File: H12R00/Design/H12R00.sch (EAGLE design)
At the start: 32 parts, among them P1 HEXABIT_17.32_NO_P3_P6, U1 STM32F091CBU6, U2 AD628ARZ, X1 XTALL_CSTCE8M00G52

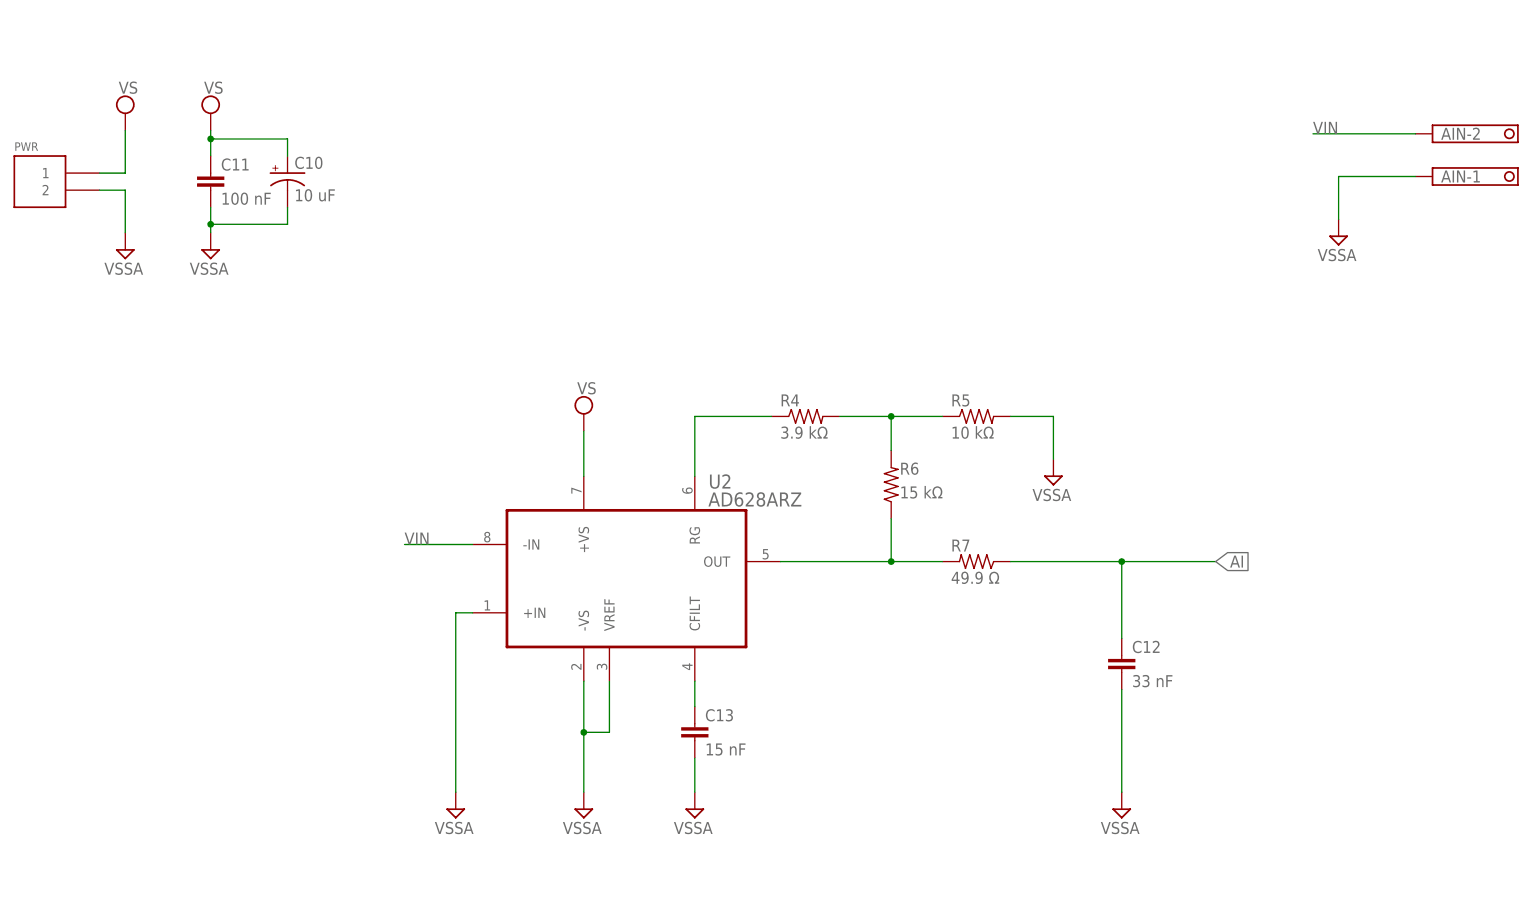
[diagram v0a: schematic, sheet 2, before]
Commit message: changed schematic design and modifies PCB (output files were not updated)
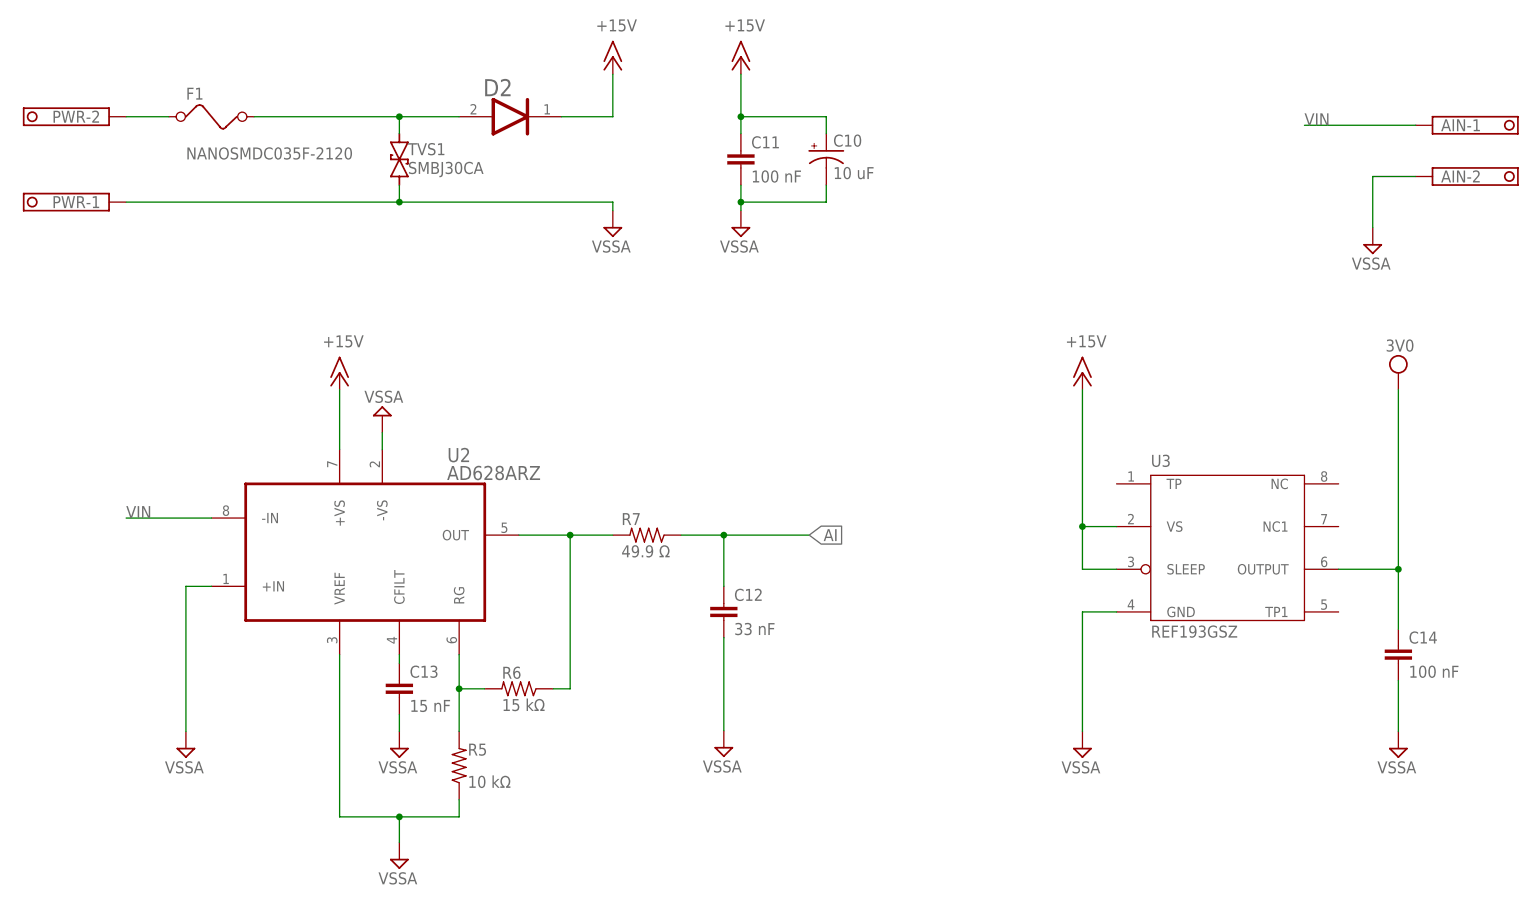
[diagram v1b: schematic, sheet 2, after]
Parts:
- removed FB1: FB-TDK_MMZ1608Y300B, Hexabitz:FB-TDK_MMZ1608Y300B
- removed R4: 3.9 kΩ, Hexabitz:R-0805
- added C14: 100 nF, Hexabitz:C-1206
- added D2: DIODES_SBR2U30P1-7DIODES_SBR2U30P1-7_0_0, Hexabitz:DIODES_SBR2U30P1-7DIODES_SBR2U30P1-7_0_0
- added F1: NANOSMDC035F-2120, Hexabitz:NANOSMDC035F-2120
- added TVS1: SMBJ30CA, Hexabitz:SMBJ30CA
- added U3: REF193GSZ, Hexabitz:REF193GSZ
- C13: CAPACITANCE 15 nF -> (none); MFN KEMET -> (none); MPN C0603C153J3GACTU -> (none); OCTOPART_URL https://octopart.com/c0603c153j3gactu-kemet-12793174 -> (none); TOLERANCE ±5% -> (none); VOLTAGE_RATING 25.0 V -> (none)
- PWR: value (none) -> CON-PHOENIX-350_1751248; device Hexabitz:1546111-2 -> Hexabitz:CON-PHOENIX-350_1751248
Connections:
- removed net AGND: AIN-1.K, C10.-, C11.2, C12.2, C13.2, PWR.2, R5.2, U2.+IN, U2.-VS, U2.VREF
- removed net VDDA: C1.1, C2.+, FB1.1, U1.VDDA
- removed net VS: C10.+, C11.1, PWR.1, U2.+VS
- new net +15V: C10.+, C11.1, D2.CATHODE, U2.+VS, U3.SLEEP, U3.VS
- new net 3V0: C1.1, C14.1, C2.+, U1.VDDA, U3.OUTPUT
- new net N$10: D2.ANODE, F1.2, TVS1.2
- net N$2: now also R5.2, R6.2; no longer R4.1
- net N$8: now also F1.1, PWR-2.K; no longer R4.2, R5.1, R6.2
- net VDD: no longer FB1.2
- net VIN: now also AIN-1.K; no longer AIN-2.K
- net VSSA: now also AIN-2.K, C10.-, C11.2, C12.2, C13.2, C14.2, PWR-1.K, R5.1, TVS1.1, U2.+IN, U2.-VS, U2.VREF, U3.GND
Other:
- note added: "+15v"
- note added: "0v"
- note added: "Analog Input (0-12v)"
- note added: "Industrial 12-Bit (0-12v) Analog Input Module"
- note removed: "Analog Input"
- note removed: "Industrial 12-Bit Analog Input Module"
- note removed: "R6 = 15k, R4 = 3.9k for Vin = 0 .. 10V"
- note removed: "R6 = 39.7k, R4 = 1.8k for Vin = 0 .. 5V"
- note removed: "Vs = 12V .. 36V for Vin = 0 .. 10V"
- note removed: "Vs = 9V .. 36V for Vin = 0 .. 5V"
- moved on the sheet: AIN-1, AIN-2, C10, C11, C12, C13, R2, R5, R6, R7, U2

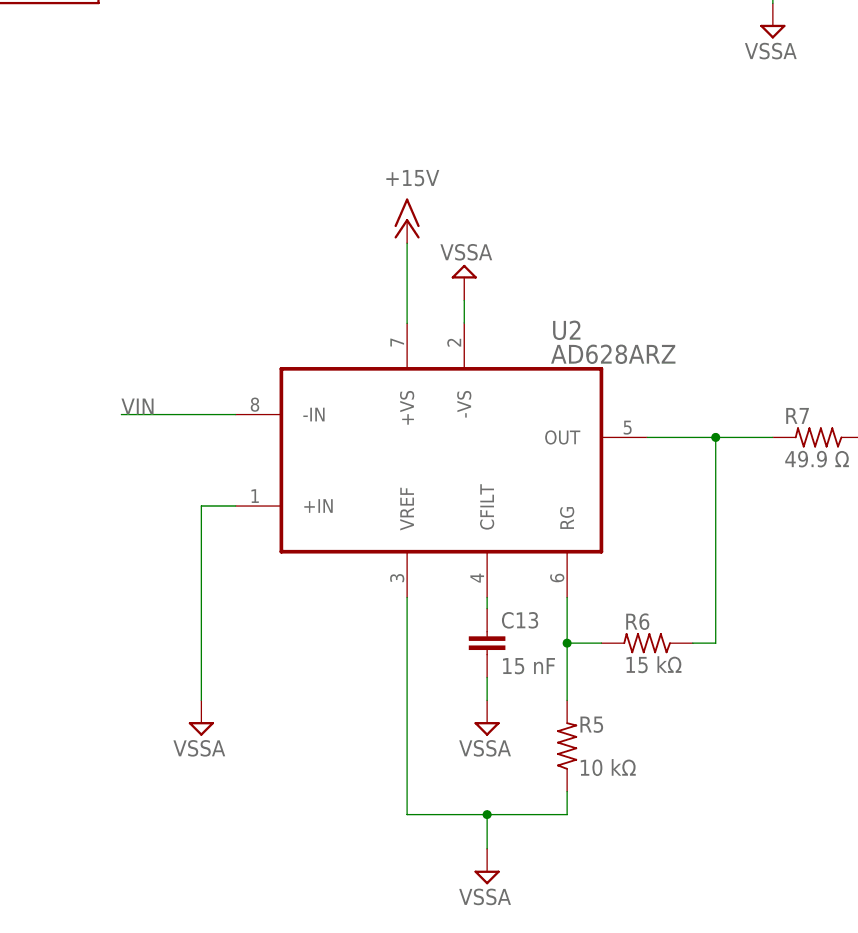
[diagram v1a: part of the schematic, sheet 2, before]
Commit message: Update some components from lib. REF is missing in lib
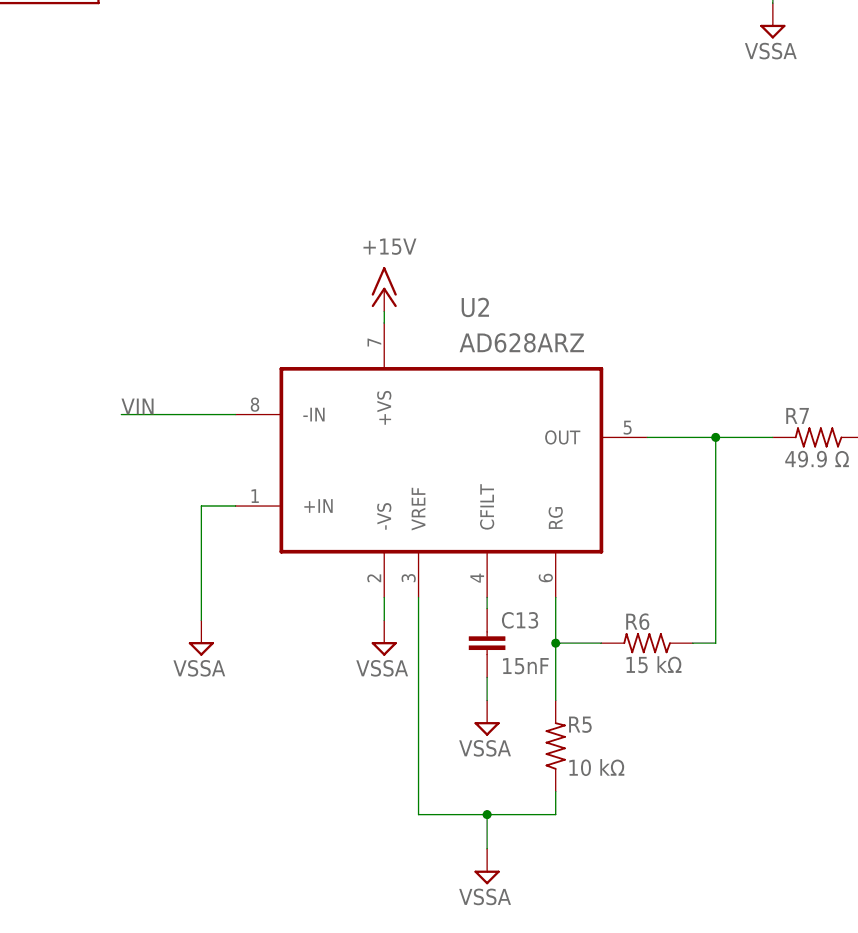
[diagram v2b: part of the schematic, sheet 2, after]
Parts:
- C13: value 15 nF -> 15nF
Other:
- moved on the sheet: R5
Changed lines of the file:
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@@
 <drawing>
 <settings>
-<setting alwaysvectorfont="no"/>
+<setting alwaysvectorfont="yes"/>
 <setting verticaltext="up"/>
 </settings>
-<grid distance="50" unitdist="mil" unit="mil" style="lines" multiple="1" display="yes" altdistance="0.01" altunitdist="inch" altunit="inch"/>
+<grid distance="50" unitdist="mil" unit="mil" style="lines" multiple="1" display="no" altdistance="0.01" altunitdist="inch" altunit="inch"/>
 <layers>
 <layer number="1" name="Top" color="4" fill="1" visible="no" active="no"/>
@@
 <part name="GND10" library="supply1" library_urn="urn:adsk.eagle:library:371" deviceset="GND" device=""/>
 <part name="AIN" library="Hexabitz" deviceset="CON-PHOENIX-350_1751248" device=""/>
-<part name="C13" library="Hexabitz" deviceset="C-0603" device="" value="15 nF"/>
+<part name="C13" library="Hexabitz" deviceset="C-0603" device="" value="15nF"/>
 <part name="SUPPLY18" library="supply2" deviceset="AGND" device="" value="VSSA"/>
 <part name="SUPPLY19" library="supply2" deviceset="AGND" device="" value="VSSA"/>
@@
 <text x="199.4662" y="19.6342" size="1.9304" layer="100" font="vector">Title</text>
 <text x="180.9242" y="19.6342" size="1.9304" layer="102" font="vector">H12R00</text>
-<text x="197.0278" y="11.8364" size="1.9304" layer="101" font="vector" align="center">Industrial 12-Bit (0-12v)
+<text x="193.2178" y="11.8364" size="1.9304" layer="101" font="vector" align="center">Industrial 12-Bit (0-12v)
 Analog Input Module</text>
 <text x="206.3242" y="19.6342" size="1.9304" layer="101" font="vector">H12R00_Backend</text>
@@
 <text x="199.4662" y="19.6342" size="1.9304" layer="100" font="vector">Title</text>
 <text x="180.9242" y="19.6342" size="1.9304" layer="102" font="vector">H12R00</text>
-<text x="197.0278" y="11.9634" size="1.9304" layer="101" font="vector" align="center">Industrial 12-Bit (0-12v)
+<text x="191.9478" y="11.9634" size="1.9304" layer="101" font="vector" align="center">Industrial 12-Bit (0-12v)
 Analog Input Module</text>
 <text x="206.3242" y="19.6342" size="1.9304" layer="101" font="vector">H12R00_Frontend</text>
@@
 </instance>
 <instance part="U2" gate="A" x="76.2" y="95.25" smashed="yes">
-<attribute name="NAME" x="93.46713125" y="108.6512" size="2.0849" layer="95" ratio="10" rot="SR0"/>
-<attribute name="VALUE" x="93.44453125" y="105.9869" size="2.08341875" layer="96" ratio="10" rot="SR0"/>
+<attribute name="NAME" x="83.30713125" y="111.1912" size="2.0849" layer="95" ratio="10" rot="SR0"/>
+<attribute name="VALUE" x="83.28453125" y="107.2569" size="2.08341875" layer="96" ratio="10" rot="SR0"/>
 </instance>
-<instance part="R5" gate="G$1" x="95.25" y="63.5" smashed="yes" rot="R90">
-<attribute name="NAME" x="96.52" y="64.9986" size="1.778" layer="95"/>
-<attribute name="VALUE" x="96.52" y="60.198" size="1.778" layer="96"/>
+<instance part="R5" gate="G$1" x="93.98" y="63.5" smashed="yes" rot="R90">
+<attribute name="NAME" x="95.25" y="64.9986" size="1.778" layer="95"/>
+<attribute name="VALUE" x="95.25" y="60.198" size="1.778" layer="96"/>
 </instance>
 <instance part="R6" gate="G$1" x="104.14" y="74.93" smashed="yes" rot="R180">
@@
 <attribute name="VALUE" x="89.027" y="64.135" size="1.778" layer="96" rot="R180"/>
 </instance>
-<instance part="SUPPLY19" gate="G$1" x="54.61" y="66.04" smashed="yes">
-<attribute name="VALUE" x="57.277" y="64.135" size="1.778" layer="96" rot="R180"/>
+<instance part="SUPPLY19" gate="G$1" x="54.61" y="74.93" smashed="yes">
+<attribute name="VALUE" x="57.277" y="73.025" size="1.778" layer="96" rot="R180"/>
 </instance>
 <instance part="PWR" gate="-1" x="43.18" y="147.32" smashed="yes" rot="R180">
@@
 <attribute name="VALUE" x="139.827" y="141.605" size="1.778" layer="96" rot="R180"/>
 </instance>
-<instance part="SUPPLY21" gate="G$1" x="83.82" y="115.57" smashed="yes" rot="R180">
-<attribute name="VALUE" x="81.153" y="117.475" size="1.778" layer="96"/>
+<instance part="SUPPLY21" gate="G$1" x="74.93" y="74.93" smashed="yes">
+<attribute name="VALUE" x="77.597" y="73.025" size="1.778" layer="96" rot="R180"/>
 </instance>
 <instance part="U3" gate="G$1" x="209.55" y="95.25" smashed="yes">
@@
 <attribute name="VALUE" x="185.42" y="125.73" size="1.778" layer="96"/>
 </instance>
-<instance part="P+4" gate="1" x="77.47" y="121.92" smashed="yes">
-<attribute name="VALUE" x="74.93" y="125.73" size="1.778" layer="96"/>
+<instance part="P+4" gate="1" x="74.93" y="114.3" smashed="yes">
+<attribute name="VALUE" x="72.39" y="118.11" size="1.778" layer="96"/>
 </instance>
 <instance part="SUPPLY7" gate="G$1" x="234.95" y="121.92" smashed="yes">
@@
 <segment>
 <pinref part="R6" gate="G$1" pin="2"/>
-<wire x1="99.06" y1="74.93" x2="95.25" y2="74.93" width="0.1524" layer="91"/>
+<wire x1="99.06" y1="74.93" x2="93.98" y2="74.93" width="0.1524" layer="91"/>
 <pinref part="U2" gate="A" pin="RG"/>
-<wire x1="95.25" y1="74.93" x2="95.25" y2="80.01" width="0.1524" layer="91"/>
+<wire x1="93.98" y1="74.93" x2="93.98" y2="80.01" width="0.1524" layer="91"/>
 <pinref part="R5" gate="G$1" pin="2"/>
-<wire x1="95.25" y1="68.58" x2="95.25" y2="74.93" width="0.1524" layer="91"/>
-<junction x="95.25" y="74.93"/>
+<wire x1="93.98" y1="68.58" x2="93.98" y2="74.93" width="0.1524" layer="91"/>
+<junction x="93.98" y="74.93"/>
 </segment>
 </net>
@@
 <pinref part="SUPPLY19" gate="G$1" pin="AGND"/>
 <pinref part="U2" gate="A" pin="+IN"/>
-<wire x1="54.61" y1="68.58" x2="54.61" y2="90.17" width="0.1524" layer="91"/>
+<wire x1="54.61" y1="77.47" x2="54.61" y2="90.17" width="0.1524" layer="91"/>
 <wire x1="54.61" y1="90.17" x2="58.42" y2="90.17" width="0.1524" layer="91"/>
 </segment>
@@
 <pinref part="U2" gate="A" pin="-VS"/>
 <pinref part="SUPPLY21" gate="G$1" pin="AGND"/>
-<wire x1="83.82" y1="110.49" x2="83.82" y2="113.03" width="0.1524" layer="91"/>
+<wire x1="74.93" y1="80.01" x2="74.93" y2="77.47" width="0.1524" layer="91"/>
 </segment>
 <segment>
@@
 <segment>
 <pinref part="R5" gate="G$1" pin="1"/>
-<wire x1="95.25" y1="58.42" x2="95.25" y2="55.88" width="0.1524" layer="91"/>
+<wire x1="93.98" y1="58.42" x2="93.98" y2="55.88" width="0.1524" layer="91"/>
 <pinref part="U2" gate="A" pin="VREF"/>
-<wire x1="95.25" y1="55.88" x2="86.36" y2="55.88" width="0.1524" layer="91"/>
-<wire x1="86.36" y1="55.88" x2="77.47" y2="55.88" width="0.1524" layer="91"/>
-<wire x1="77.47" y1="55.88" x2="77.47" y2="80.01" width="0.1524" layer="91"/>
+<wire x1="93.98" y1="55.88" x2="86.36" y2="55.88" width="0.1524" layer="91"/>
+<wire x1="86.36" y1="55.88" x2="78.74" y2="55.88" width="0.1524" layer="91"/>
+<wire x1="78.74" y1="55.88" x2="78.74" y2="80.01" width="0.1524" layer="91"/>
 <wire x1="86.36" y1="52.07" x2="86.36" y2="55.88" width="0.1524" layer="91"/>
 <junction x="86.36" y="55.88"/>
@@
 <segment>
 <pinref part="U2" gate="A" pin="+VS"/>
-<wire x1="77.47" y1="110.49" x2="77.47" y2="119.38" width="0.1524" layer="91"/>
+<wire x1="74.93" y1="110.49" x2="74.93" y2="111.76" width="0.1524" layer="91"/>
 <pinref part="P+4" gate="1" pin="+15V"/>
 </segment>
